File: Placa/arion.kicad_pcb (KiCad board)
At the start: 2 copper layers, 70.5 x 78.7 mm, 33 parts, among them P1 CONN_01X03, P2 CONN_01X02, P3 CONN_01X06, SW1 SW_PUSH, SW2 SW_PUSH, SW3 SW_PUSH, U1 TCRT1000, U2 TCRT1000, U3 TCRT1000, U4 TCRT1000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

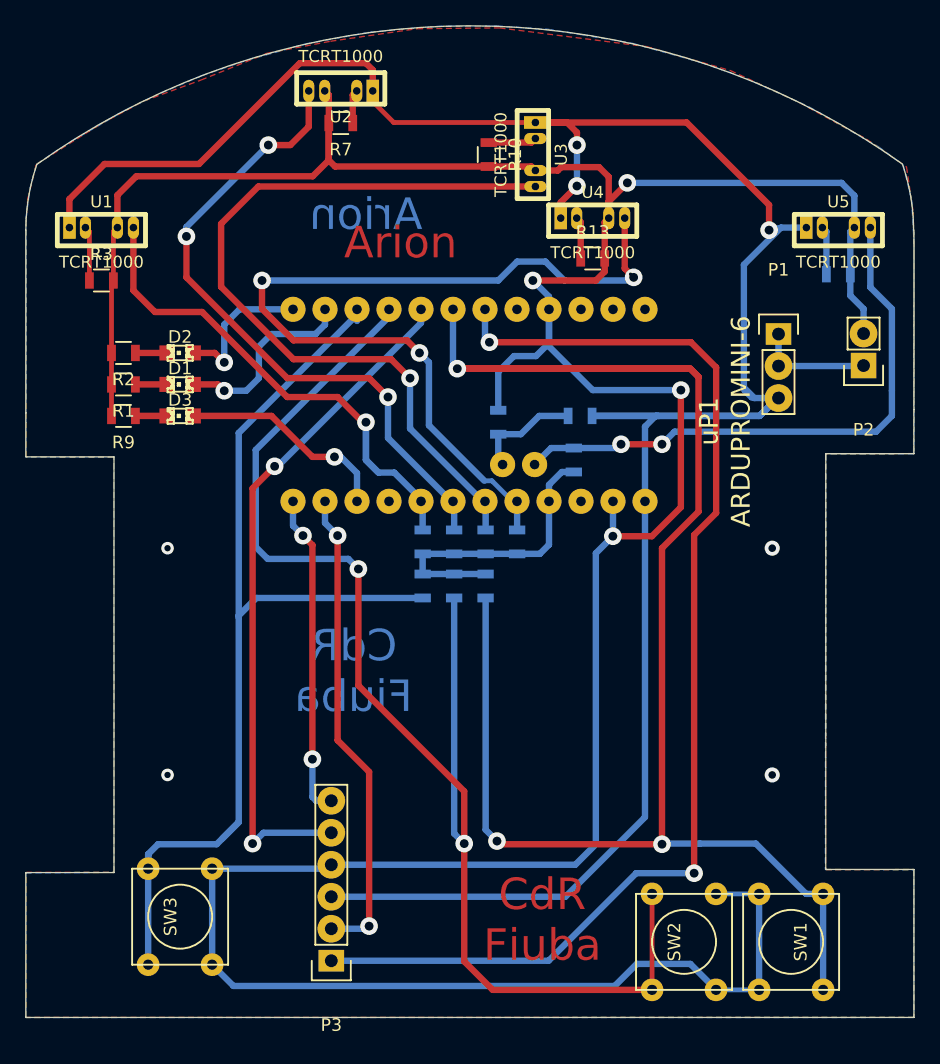
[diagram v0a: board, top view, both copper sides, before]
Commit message: Se cambiaron los errores que habia en la ultima version
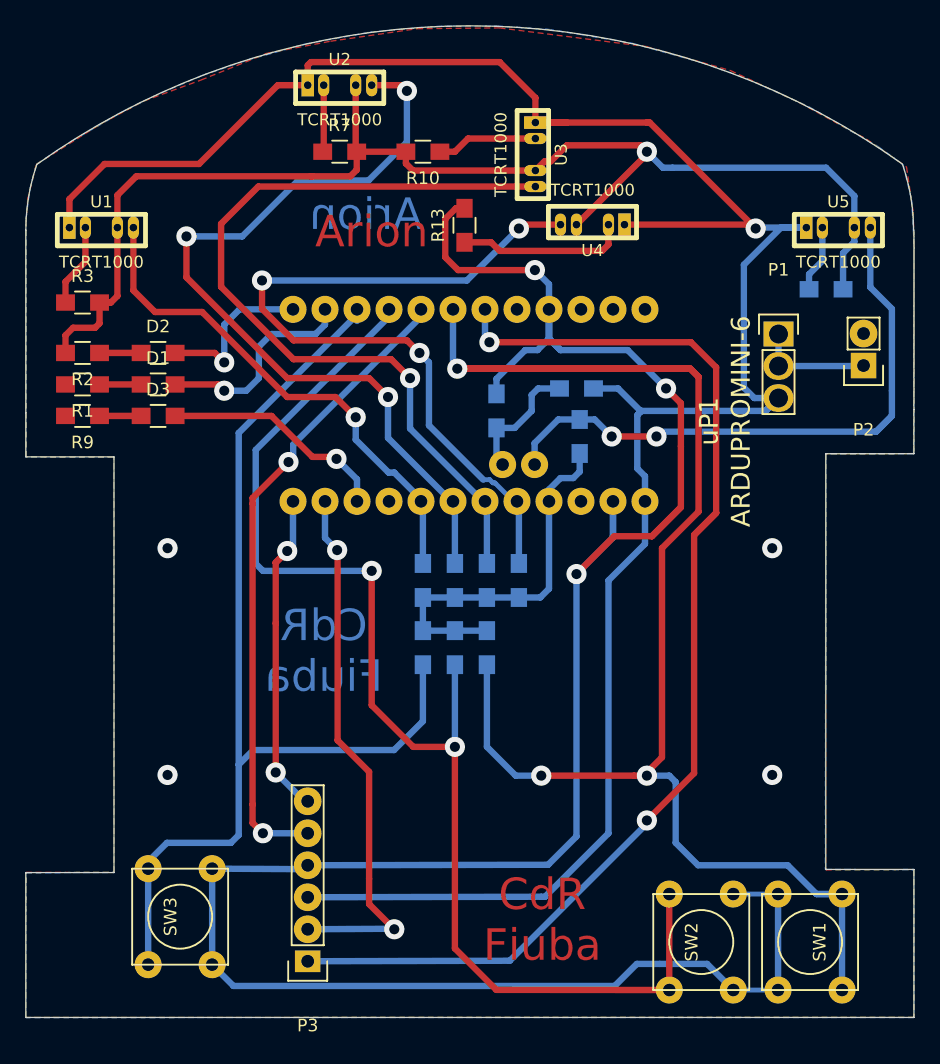
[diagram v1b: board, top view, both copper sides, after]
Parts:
- D1, D2, D3: footprint LEDs:LED-0805 -> Resistors_SMD:R_0805_HandSoldering
- R1, R10, R11, R12, R13, R14, R15, R16, R17, R18, R2, R3, R4, R5, R6, R7, R8, R9: footprint Resistors_SMD:R_0805 -> Resistors_SMD:R_0805_HandSoldering
- moved R13 10.5 mm to (99.8, 55.1), turned to 90 degrees
- moved R10 5.23 mm to (96.5, 49.3), turned to 180 degrees
- moved R12 4.90 mm to (101.6, 88.6)
- moved R15 4.90 mm to (99.1, 88.6)
- moved R18 4.90 mm to (96.5, 88.6)
- moved R1 3.25 mm to (69.5, 67.8)
- moved R2 3.25 mm to (69.5, 65.2)
- moved R9 3.25 mm to (69.5, 70.2)
- moved R14 3.07 mm to (104.1, 83.3)
- moved R11 3.06 mm to (101.6, 83.3)
- moved R8 3.06 mm to (99.1, 83.3)
- moved R4 3.06 mm to (96.5, 83.3)
- moved R3 2.30 mm to (69.5, 61.2)
- moved R7 2.28 mm to (89.9, 49.3), turned to 0 degrees
- moved R5 2.20 mm to (108.7, 68.1)
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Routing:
- net +8V: track 222.1 -> 183.3 mm, vias 3 -> 1
- net /Boton3: track 101.8 -> 84.2 mm
- net /Boton2: track 118.7 -> 101.2 mm
- net /A1: track 54.8 -> 68.7 mm
- net Net-(R13-Pad1): track 3.79 -> 13.5 mm
- net /Boton1: track 138.2 -> 129.1 mm
- net /A3: track 71.8 -> 64.0 mm, vias 4 -> 3
- net /SentidoMotor2: track 58.8 -> 51.5 mm
- net GND: track 304.3 -> 297.9 mm
- net Net-(R10-Pad1): track 4.29 -> 8.01 mm
- net Net-(D2-Pad2): track 14.5 -> 18.0 mm
- net /Motor1: track 40.9 -> 44.1 mm
- net /A2: track 90.0 -> 92.8 mm
- net Net-(D3-Pad2): track 17.4 -> 19.8 mm
- net /A0: track 43.5 -> 41.3 mm
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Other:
- net class Default: via_dia 1.4 -> 1.6; via_drill 1 -> 0.8
